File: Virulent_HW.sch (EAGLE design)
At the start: 54 parts, among them U1 STM32F050G6U6

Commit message: Added SWD connector, Bulk input capacitance.
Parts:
- added C26: 10u, rcl:C-EUC1206
- added JP1: (no value), Virulent_HW:PINHD-1X6
- added R18, R20, R21: 22, Virulent_HW:R-US_R0402
- added R19: NU, Virulent_HW:R-US_R0402
- R11: value 10k -> 30
- R12: value 10k -> 120
- R13: value 10k -> 39.2
- R15, R17: value NU -> 10k
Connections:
- new net STM_SWCLK: R21.2, U1-IO.PA14@22
- new net STM_SWDAT: R20.2, U1-IO.PA13@21
- new net STM_SWO: R19.2, U1-IO.PA15@23
- new net SWD_NRST: JP1.1, R18.1
- new net SWD_SWCLK: JP1.4, R21.1
- new net SWD_SWDAT: JP1.3, R20.1
- new net SWD_SWO: JP1.2, R19.1
- net +3.3V: now also JP1.6
- net +9-36V: now also C26.2
- net GND: now also C26.1, JP1.5
- net N$6: now also R18.2
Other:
- note added: "SWD"
- note added: "Version 1.0"
- note removed: "Version 12"
- moved on the sheet: C4, C5, C6, C7, C8, R10, R11, R13, R9, U1-PWR/CTRL, VR1

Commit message: Updated reciever and PLL circuitry. Added hard and soft reset buttons.
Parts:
- added C27: 1n, rcl:C-EUC1206
- added C28: NU, rcl:C-EUC1206
- added D1: NTE583, Virulent_HW:NTE583
- added R22, R24: 10k, Virulent_HW:R-US_R0402
- added R23: 15k, Virulent_HW:R-US_R0402
- added R25: 6.8k, Virulent_HW:R-US_R0402
- added R26, R28: 1Meg, Virulent_HW:R-US_R0402
- added R27: 5.6Meg, Virulent_HW:R-US_R0402
- added SW1: COM08229, Virulent_HW:COM08229
- added SW2: COM08720, Virulent_HW:COM08720
- C1, C2, C3: value (none) -> 0.1u
- C13: value (none) -> 250u
- C14, C15, C16: value (none) -> 2.2u
- C17, C18, C19, C20, C21: value (none) -> 1n
- R1, R2, R3: value (none) -> 4.7k
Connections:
- new net N$27: PLL3.TIMING_CAPACITOR@6, R25.2
- new net N$29: D1.ANNODE@1, NFC1.1@1, R26.2, R27.1
- new net RESET: R22.1, SW1.2@2, U1-IO.PA2@8
- net +3.3V: now also R22.2
- net +5V: now also C17.2, C18.2, C19.2, R27.2; no longer C16.1, C20.1, C3.1, PLL3.V+@4
- net GND: now also C1.1, C13.1, C14.1, C15.1, C16.1, C17.1, C18.1, C19.1, C2.1, C20.1, C21.1, C27.1, C28.2, C3.1, R26.1, R28.1, SW1.1@1, SW2.3@3, SW2.4@4; no longer C1.2, C13.2, C14.2, C15.2, C16.2, C17.2, C18.2, C19.2, C2.2, C20.2, C21.2, C3.2
- net N$1: now also C1.2, PLL1.LOOP_FILTER@2, R1.2; no longer C1.1, PLL1.OUTPUT_FILTER@1
- net N$10: now also C15.2, PLL2.OUTPUT_FILTER@1; no longer C17.1, PLL2.TIMING_RESISTOR@5, R2.1
- net N$12: now also C21.2, PLL2.TIMING_RESISTOR@5, R24.1; no longer C18.1, PLL3.OUTPUT_FILTER@1
- net N$13: now also PLL1.TIMING_CAPACITOR@6, R23.2; no longer PLL3.TIMING_CAPACITOR@6, R3.2
- net N$14: now also PLL2.TIMING_CAPACITOR@6, R24.2; no longer C19.1, PLL3.LOOP_FILTER@2
- net N$17: now also C27.2, R25.1; no longer C21.1, R3.1
- net N$2: now also C2.2, PLL2.LOOP_FILTER@2, R2.2; no longer C14.1, PLL2.OUTPUT_FILTER@1
- net N$3: now also C3.2, PLL3.LOOP_FILTER@2, R3.2; no longer PLL1.TIMING_CAPACITOR@6, R1.2
- net N$4: now also C13.2, R2.1, R3.1; no longer C13.1, PLL1.TIMING_RESISTOR@5
- net N$5: now also C14.2, PLL1.OUTPUT_FILTER@1; no longer C2.1, PLL1.LOOP_FILTER@2
- net N$6: now also SW2.1@1, SW2.2@2
- net N$7: now also C16.2, PLL3.OUTPUT_FILTER@1; no longer PLL2.TIMING_CAPACITOR@6, R2.2
- net N$8: now also C20.2, PLL1.TIMING_RESISTOR@5, R23.1; no longer C15.1, PLL2.LOOP_FILTER@2
- net NFC: now also C28.1, D1.CATHODE@2, R28.2; no longer NFC1.1@1
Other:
- note added: "1477 Hz"
- note added: "697 Hz"
- note added: "941 Hz"
- note added: "Reciever"
- note removed: "2kHz PLL"
- note removed: "3kHz PLL"
- note removed: "5kHz PLL"
- note removed: "NFC Transmitter"
- moved on the sheet: C1, C13, C14, C15, C16, C17, C18, C19, C2, C20, C21, C25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

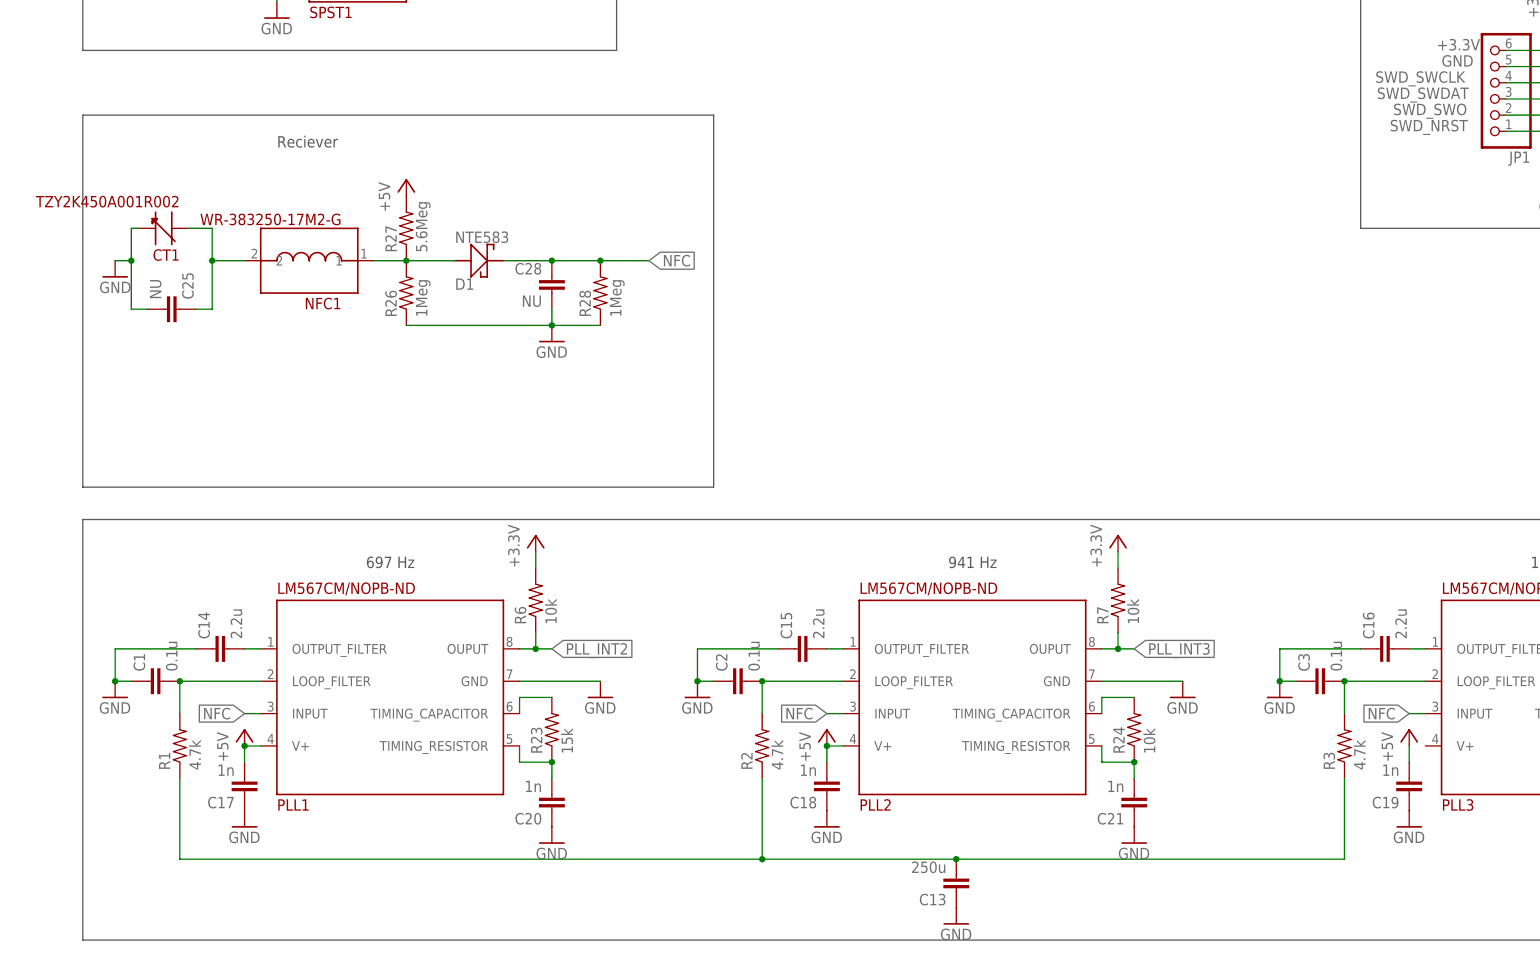
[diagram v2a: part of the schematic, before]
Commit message: updated package size for 250y Capacitor
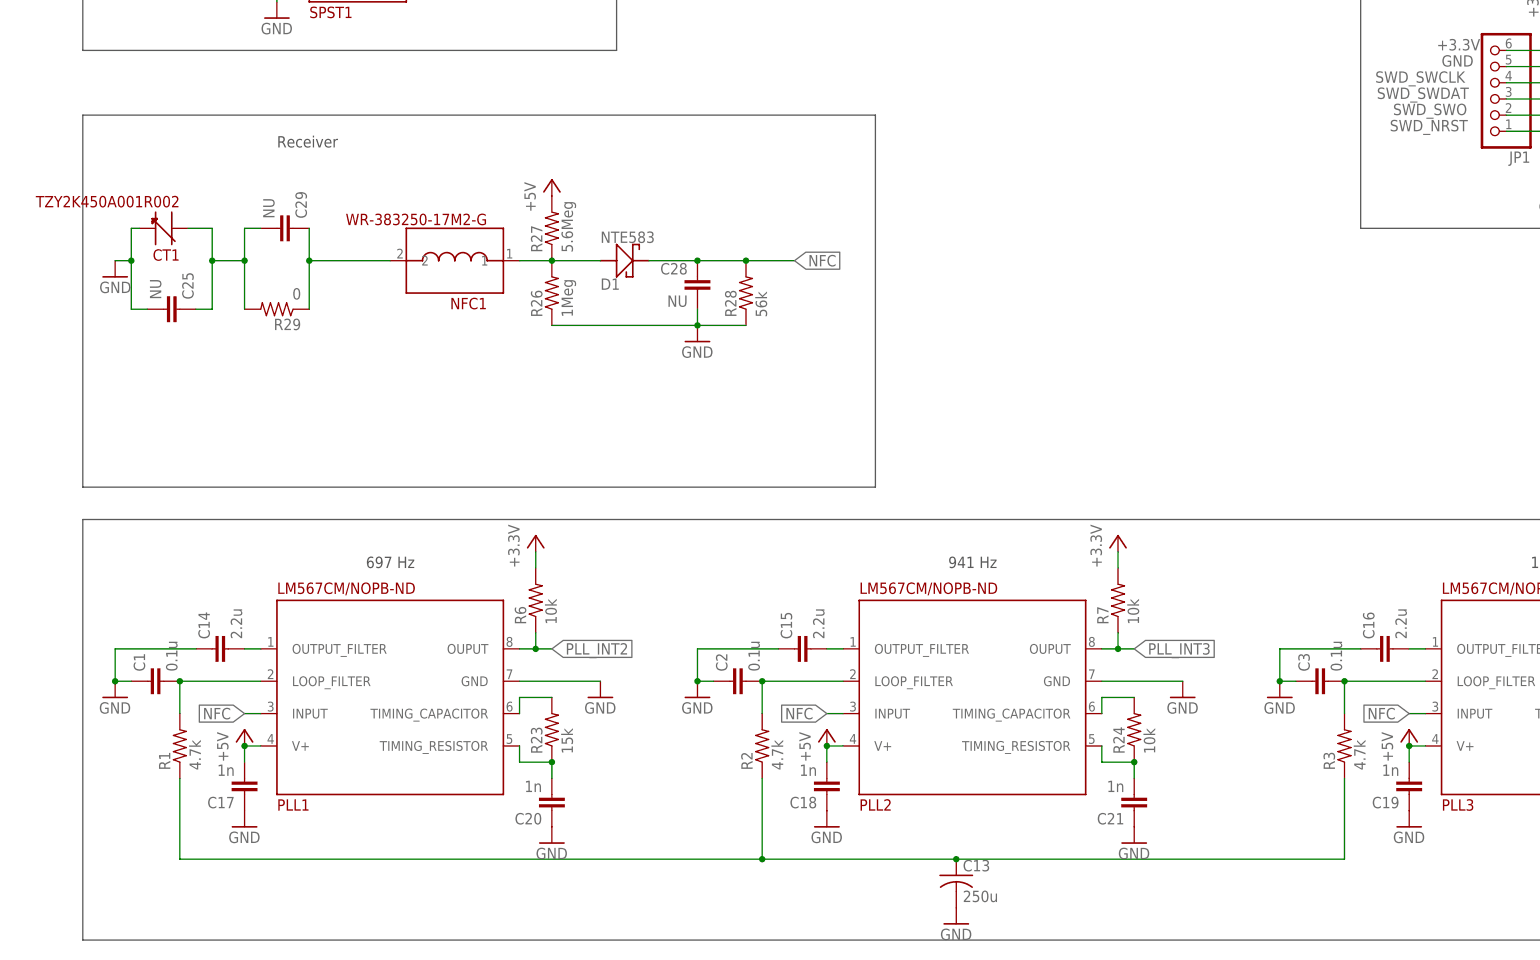
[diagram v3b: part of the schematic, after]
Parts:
- added C29: NU, rcl:C-EUC1206
- added R29: 0, Virulent_HW:R-US_R0402
- C13: device rcl:C-EUC1206 -> rcl:C-USC1210
- R28: value 1Meg -> 56k
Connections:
- new net N$30: C29.1, NFC1.2@2, R29.1
- net +5V: now also PLL3.V+@4
- net GND: now also C13.2; no longer C13.1
- net N$26: now also C29.2, R29.2; no longer NFC1.2@2
- net N$4: now also C13.1; no longer C13.2
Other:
- note added: "Receiver"
- note removed: "Reciever"
- moved on the sheet: C13, C28, D1, NFC1, R26, R27, R28
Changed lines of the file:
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@@
 <setting verticaltext="up"/>
 </settings>
-<grid distance="0.05" unitdist="inch" unit="inch" style="lines" multiple="1" display="no" altdistance="0.01" altunitdist="inch" altunit="inch"/>
+<grid distance="0.1" unitdist="inch" unit="inch" style="lines" multiple="1" display="no" altdistance="0.01" altunitdist="inch" altunit="inch"/>
 <layers>
 <layer number="1" name="Top" color="4" fill="1" visible="no" active="no"/>
@@
 <part name="C3" library="rcl" deviceset="C-EU" device="C1206" value="0.1u"/>
 <part name="R3" library="Virulent_HW" deviceset="R-US_" device="R0402" value="4.7k"/>
-<part name="C13" library="rcl" deviceset="C-EU" device="C1206" value="250u"/>
 <part name="GND25" library="Virulent_HW" deviceset="GND" device=""/>
 <part name="GND6" library="Virulent_HW" deviceset="GND" device=""/>
@@
 <part name="P+21" library="Virulent_HW" deviceset="+5V" device=""/>
 <part name="C28" library="rcl" deviceset="C-EU" device="C1206" value="NU"/>
-<part name="R28" library="Virulent_HW" deviceset="R-US_" device="R0402" value="1Meg"/>
+<part name="R28" library="Virulent_HW" deviceset="R-US_" device="R0402" value="56k"/>
 <part name="D1" library="Virulent_HW" deviceset="NTE583" device=""/>
+<part name="C29" library="rcl" deviceset="C-EU" device="C1206" value="NU"/>
+<part name="R29" library="Virulent_HW" deviceset="R-US_" device="R0402" value="0"/>
+<part name="C13" library="rcl" deviceset="C-US" device="C1210" value="250u"/>
 </parts>
 <sheets>
@@
 <wire x1="10.16" y1="147.32" x2="10.16" y2="182.88" width="0.1524" layer="97"/>
 <text x="40.64" y="177.8" size="1.778" layer="97">Frequency Modulation</text>
-<wire x1="10.16" y1="137.16" x2="109.22" y2="137.16" width="0.1524" layer="97"/>
-<wire x1="109.22" y1="137.16" x2="109.22" y2="78.74" width="0.1524" layer="97"/>
-<wire x1="109.22" y1="78.74" x2="10.16" y2="78.74" width="0.1524" layer="97"/>
+<wire x1="10.16" y1="137.16" x2="134.62" y2="137.16" width="0.1524" layer="97"/>
+<wire x1="134.62" y1="137.16" x2="134.62" y2="78.74" width="0.1524" layer="97"/>
+<wire x1="134.62" y1="78.74" x2="10.16" y2="78.74" width="0.1524" layer="97"/>
 <wire x1="10.16" y1="78.74" x2="10.16" y2="137.16" width="0.1524" layer="97"/>
-<text x="40.64" y="132.08" size="1.778" layer="97">Reciever</text>
+<text x="40.64" y="132.08" size="1.778" layer="97">Receiver</text>
 <text x="12.7" y="215.9" size="1.778" layer="97" rot="R90">Power Supply</text>
 <text x="149.86" y="248.92" size="5.08" layer="97">Virulent</text>
@@
 <instance part="CT1" gate="G$1" x="22.86" y="119.38" rot="MR0"/>
 <instance part="GND19" gate="1" x="15.24" y="111.76" rot="MR0"/>
-<instance part="NFC1" gate="G$1" x="45.72" y="114.3" rot="MR0"/>
+<instance part="NFC1" gate="G$1" x="68.58" y="114.3" rot="MR0"/>
 <instance part="C25" gate="G$1" x="25.4" y="106.68" rot="MR90"/>
 <instance part="P+18" gate="1" x="71.12" y="170.18"/>
@@
 <instance part="C3" gate="G$1" x="203.2" y="48.26" rot="R90"/>
 <instance part="R3" gate="G$1" x="208.28" y="38.1" rot="R90"/>
-<instance part="C13" gate="G$1" x="147.32" y="15.24" rot="R180"/>
 <instance part="GND25" gate="1" x="147.32" y="10.16"/>
 <instance part="GND6" gate="1" x="15.24" y="45.72"/>
@@
 <instance part="C27" gate="G$1" x="266.7" y="27.94" rot="R180"/>
 <instance part="GND34" gate="1" x="266.7" y="22.86"/>
-<instance part="GND35" gate="1" x="83.82" y="101.6"/>
-<instance part="R26" gate="G$1" x="60.96" y="109.22" rot="R90"/>
-<instance part="R27" gate="G$1" x="60.96" y="119.38" rot="R90"/>
-<instance part="P+21" gate="1" x="60.96" y="127"/>
-<instance part="C28" gate="G$1" x="83.82" y="111.76" rot="MR0"/>
-<instance part="R28" gate="G$1" x="91.44" y="109.22" rot="R90"/>
-<instance part="D1" gate="G$1" x="73.66" y="114.3"/>
+<instance part="GND35" gate="1" x="106.68" y="101.6"/>
+<instance part="R26" gate="G$1" x="83.82" y="109.22" rot="R90"/>
+<instance part="R27" gate="G$1" x="83.82" y="119.38" rot="R90"/>
+<instance part="P+21" gate="1" x="83.82" y="127"/>
+<instance part="C28" gate="G$1" x="106.68" y="111.76" rot="MR0"/>
+<instance part="R28" gate="G$1" x="114.3" y="109.22" rot="R90"/>
+<instance part="D1" gate="G$1" x="96.52" y="114.3"/>
+<instance part="C29" gate="G$1" x="43.18" y="119.38" rot="MR90"/>
+<instance part="R29" gate="G$1" x="40.64" y="106.68" rot="R180"/>
+<instance part="C13" gate="G$1" x="147.32" y="17.78"/>
 </instances>
 <busses>
@@
 <wire x1="218.44" y1="38.1" x2="218.44" y2="35.56" width="0.1524" layer="91"/>
 <pinref part="C19" gate="G$1" pin="2"/>
+<pinref part="PLL3" gate="G$1" pin="V+@4"/>
+<wire x1="220.98" y1="38.1" x2="218.44" y2="38.1" width="0.1524" layer="91"/>
+<junction x="218.44" y="38.1"/>
 </segment>
 <segment>
@@
 </segment>
 <segment>
-<pinref part="C13" gate="G$1" pin="1"/>
-<pinref part="GND25" gate="1" pin="GND"/>
-</segment>
-<segment>
 <pinref part="C1" gate="G$1" pin="1"/>
 <wire x1="17.78" y1="48.26" x2="15.24" y2="48.26" width="0.1524" layer="91"/>
@@
 <pinref part="R26" gate="G$1" pin="1"/>
 <pinref part="R28" gate="G$1" pin="1"/>
-<wire x1="60.96" y1="104.14" x2="83.82" y2="104.14" width="0.1524" layer="91"/>
+<wire x1="83.82" y1="104.14" x2="106.68" y2="104.14" width="0.1524" layer="91"/>
 <pinref part="C28" gate="G$1" pin="2"/>
-<wire x1="83.82" y1="104.14" x2="91.44" y2="104.14" width="0.1524" layer="91"/>
-<wire x1="83.82" y1="106.68" x2="83.82" y2="104.14" width="0.1524" layer="91"/>
+<wire x1="106.68" y1="104.14" x2="114.3" y2="104.14" width="0.1524" layer="91"/>
+<wire x1="106.68" y1="106.68" x2="106.68" y2="104.14" width="0.1524" layer="91"/>
 <pinref part="GND35" gate="1" pin="GND"/>
-<junction x="83.82" y="104.14"/>
+<junction x="106.68" y="104.14"/>
 </segment>
 <segment>
@@
 <pinref part="GND31" gate="1" pin="GND"/>
 <wire x1="261.62" y1="48.26" x2="271.78" y2="48.26" width="0.1524" layer="91"/>
+</segment>
+<segment>
+<pinref part="GND25" gate="1" pin="GND"/>
+<pinref part="C13" gate="G$1" pin="2"/>
 </segment>
 </net>
@@
 </segment>
 <segment>
-<label x="99.06" y="114.3" size="1.778" layer="95" rot="MR180" xref="yes"/>
+<label x="121.92" y="114.3" size="1.778" layer="95" rot="MR180" xref="yes"/>
 <pinref part="C28" gate="G$1" pin="1"/>
-<wire x1="83.82" y1="114.3" x2="91.44" y2="114.3" width="0.1524" layer="91"/>
+<wire x1="106.68" y1="114.3" x2="114.3" y2="114.3" width="0.1524" layer="91"/>
 <pinref part="R28" gate="G$1" pin="2"/>
-<wire x1="91.44" y1="114.3" x2="99.06" y2="114.3" width="0.1524" layer="91"/>
-<junction x="91.44" y="114.3"/>
+<wire x1="114.3" y1="114.3" x2="121.92" y2="114.3" width="0.1524" layer="91"/>
+<junction x="114.3" y="114.3"/>
 <pinref part="D1" gate="G$1" pin="CATHODE@2"/>
-<wire x1="76.2" y1="114.3" x2="83.82" y2="114.3" width="0.1524" layer="91"/>
-<junction x="83.82" y="114.3"/>
+<wire x1="99.06" y1="114.3" x2="106.68" y2="114.3" width="0.1524" layer="91"/>
+<junction x="106.68" y="114.3"/>
 </segment>
 <segment>
@@
 <wire x1="30.48" y1="106.68" x2="27.94" y2="106.68" width="0.1524" layer="91"/>
 <pinref part="C25" gate="G$1" pin="1"/>
-<pinref part="NFC1" gate="G$1" pin="2@2"/>
-<wire x1="35.56" y1="114.3" x2="30.48" y2="114.3" width="0.1524" layer="91"/>
+<wire x1="30.48" y1="114.3" x2="35.56" y2="114.3" width="0.1524" layer="91"/>
+<wire x1="35.56" y1="114.3" x2="35.56" y2="119.38" width="0.1524" layer="91"/>
+<wire x1="35.56" y1="119.38" x2="38.1" y2="119.38" width="0.1524" layer="91"/>
+<pinref part="C29" gate="G$1" pin="2"/>
+<pinref part="R29" gate="G$1" pin="2"/>
+<wire x1="35.56" y1="114.3" x2="35.56" y2="106.68" width="0.1524" layer="91"/>
 <junction x="30.48" y="114.3"/>
+<junction x="35.56" y="114.3"/>
 </segment>
 </net>
@@
 <pinref part="R2" gate="G$1" pin="1"/>
 <wire x1="116.84" y1="20.32" x2="116.84" y2="33.02" width="0.1524" layer="91"/>
+<pinref part="R3" gate="G$1" pin="1"/>
 <wire x1="116.84" y1="20.32" x2="147.32" y2="20.32" width="0.1524" layer="91"/>
-<pinref part="R3" gate="G$1" pin="1"/>
 <wire x1="147.32" y1="20.32" x2="208.28" y2="20.32" width="0.1524" layer="91"/>
 <wire x1="208.28" y1="20.32" x2="208.28" y2="33.02" width="0.1524" layer="91"/>
-<pinref part="C13" gate="G$1" pin="2"/>
+<junction x="116.84" y="20.32"/>
+<pinref part="C13" gate="G$1" pin="1"/>
 <junction x="147.32" y="20.32"/>
-<junction x="116.84" y="20.32"/>
 </segment>
 </net>
@@
 <segment>
 <pinref part="R27" gate="G$1" pin="1"/>
-<junction x="60.96" y="114.3"/>
+<junction x="83.82" y="114.3"/>
 <pinref part="R26" gate="G$1" pin="2"/>
-<wire x1="55.88" y1="114.3" x2="60.96" y2="114.3" width="0.1524" layer="91"/>
+<wire x1="78.74" y1="114.3" x2="83.82" y2="114.3" width="0.1524" layer="91"/>
 <pinref part="NFC1" gate="G$1" pin="1@1"/>
 <pinref part="D1" gate="G$1" pin="ANNODE@1"/>
-<wire x1="60.96" y1="114.3" x2="68.58" y2="114.3" width="0.1524" layer="91"/>
+<wire x1="83.82" y1="114.3" x2="91.44" y2="114.3" width="0.1524" layer="91"/>
 </segment>
 </net>
@@
 </segment>
 </net>
+<net name="N$30" class="0">
+<segment>
+<pinref part="R29" gate="G$1" pin="1"/>
+<pinref part="C29" gate="G$1" pin="1"/>
+<wire x1="45.72" y1="106.68" x2="45.72" y2="114.3" width="0.1524" layer="91"/>
+<pinref part="NFC1" gate="G$1" pin="2@2"/>
+<wire x1="45.72" y1="114.3" x2="45.72" y2="119.38" width="0.1524" layer="91"/>
+<wire x1="45.72" y1="114.3" x2="58.42" y2="114.3" width="0.1524" layer="91"/>
+<junction x="45.72" y="114.3"/>
+</segment>
+</net>
